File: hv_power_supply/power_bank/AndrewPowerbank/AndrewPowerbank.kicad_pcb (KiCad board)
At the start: 2 copper layers, 48.3 x 30.5 mm, 53 parts, among them J1 NanoFit_RA_TH_02, J2 NanoFit_RA_TH_02, J3 USB-A-S-X-X-SM2, J4 USB-Micro-1981568-1, J5 NanoFit_RA_TH_02, Q1 SSM3K333R, U1 MCP73871T-2CCI_ML, U2 TPS61090RSAR

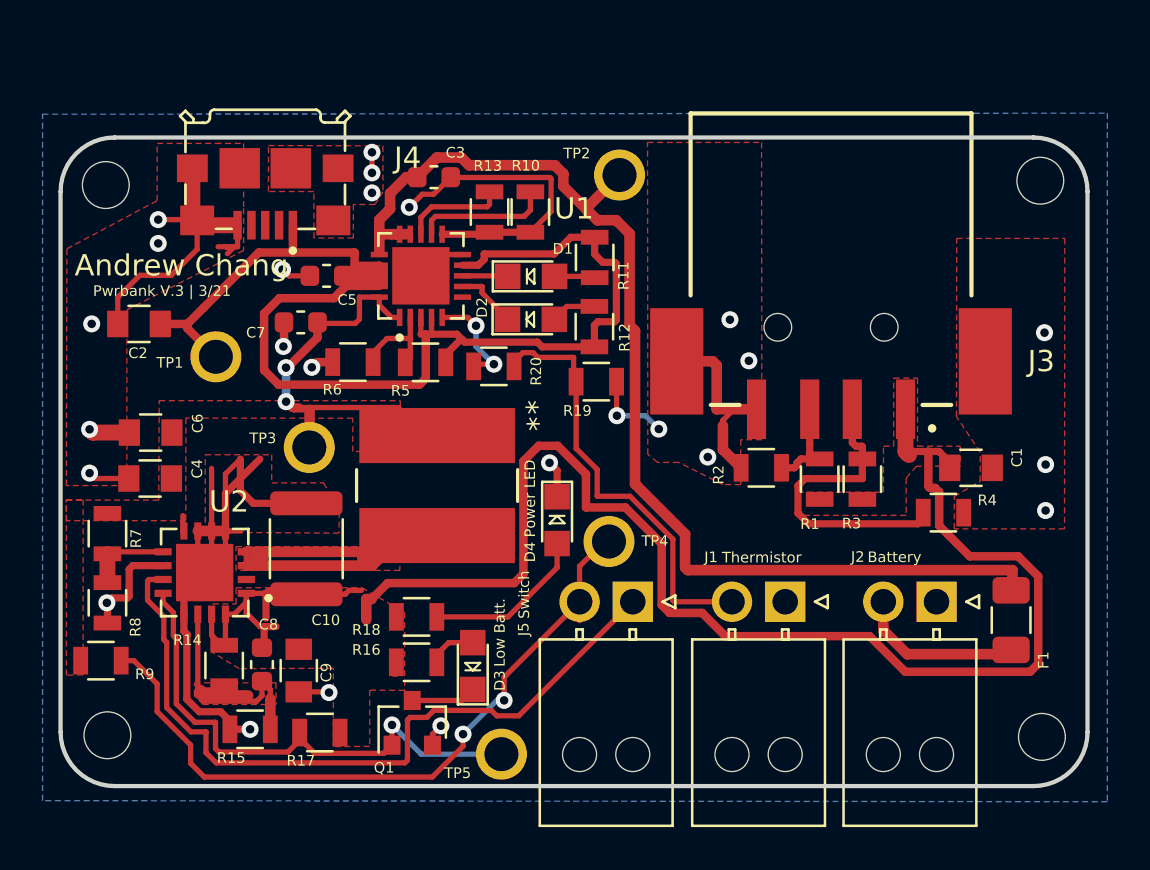
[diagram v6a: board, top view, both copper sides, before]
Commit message: Adjust component labels, back silkscreen.
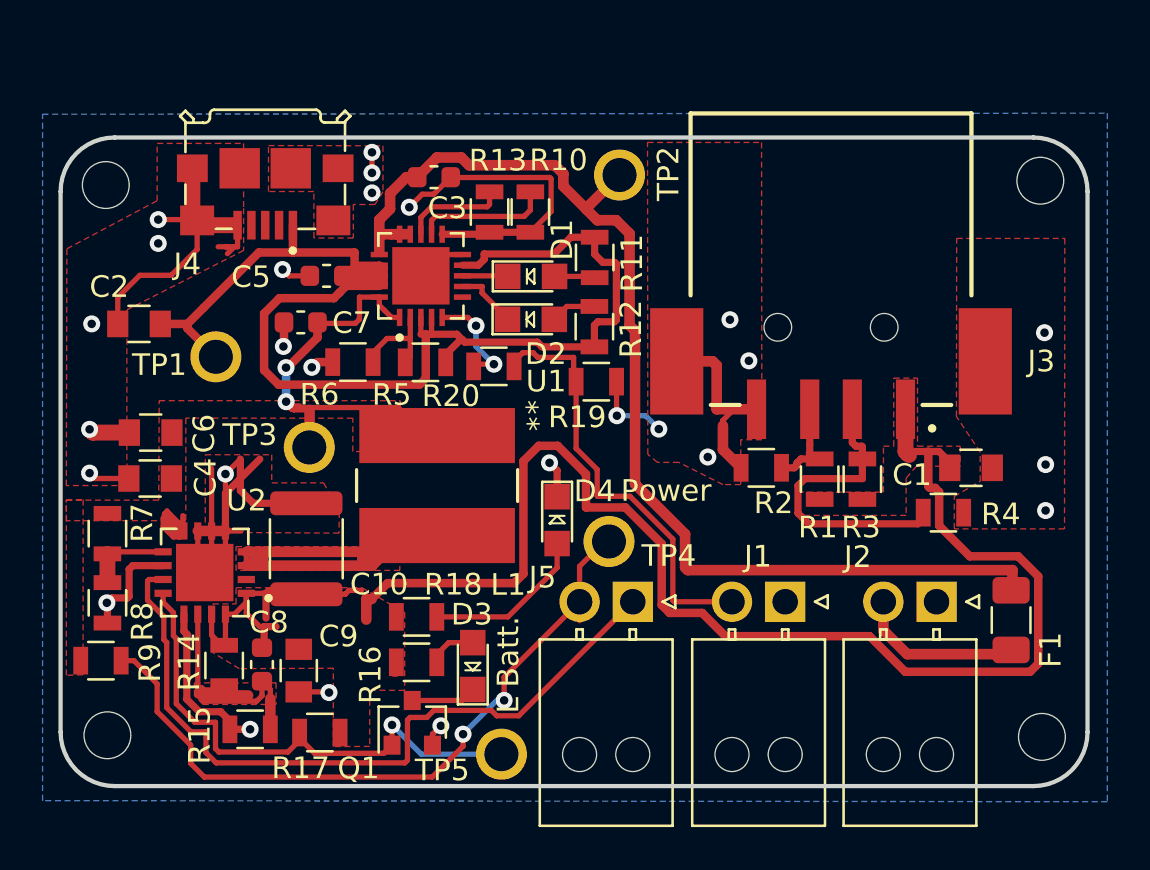
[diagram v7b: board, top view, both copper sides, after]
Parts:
- added G***: LOGO, footprints:Small_OE_Logo, B.Cu at (44.5, 94.0)
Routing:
- net +BATT: track 21.8 -> 26.4 mm
- net GND: track 101.7 -> 100.8 mm, vias 25 -> 26
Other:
- board text added: "D1: Low Battery Output D2: Charge Complete"
- board text added: "L Batt."
- board text added: "Power"
- board text added: "Powerbank V.4 | 4/18/21"
- board text removed: "Low Batt."
- board text removed: "Power LED"
- board text removed: "Pwrbank V.3 | 3/21"
